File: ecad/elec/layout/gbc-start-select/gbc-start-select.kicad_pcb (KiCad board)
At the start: 2 copper layers, 5 parts

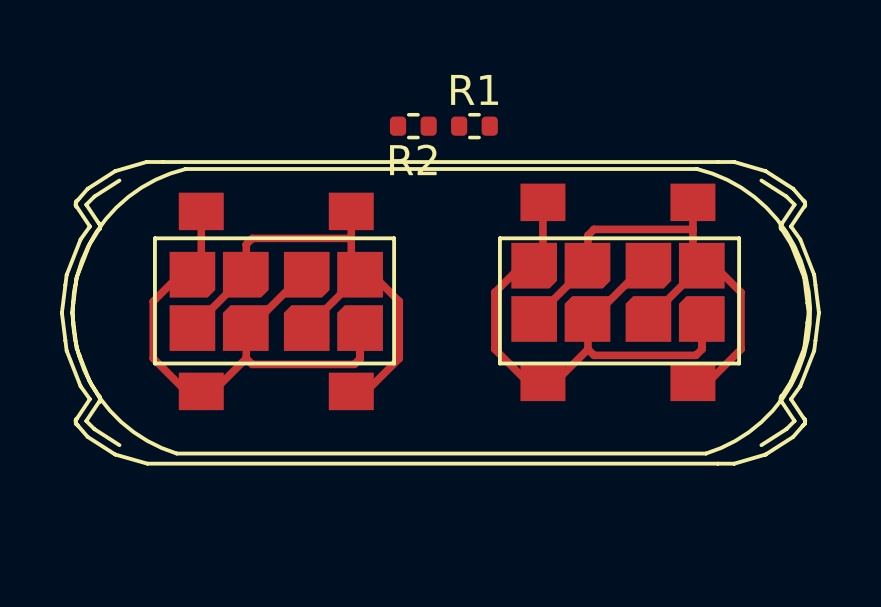
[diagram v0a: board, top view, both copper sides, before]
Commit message: update layouts to use latest footprints and fixed volume buttons and include address pins
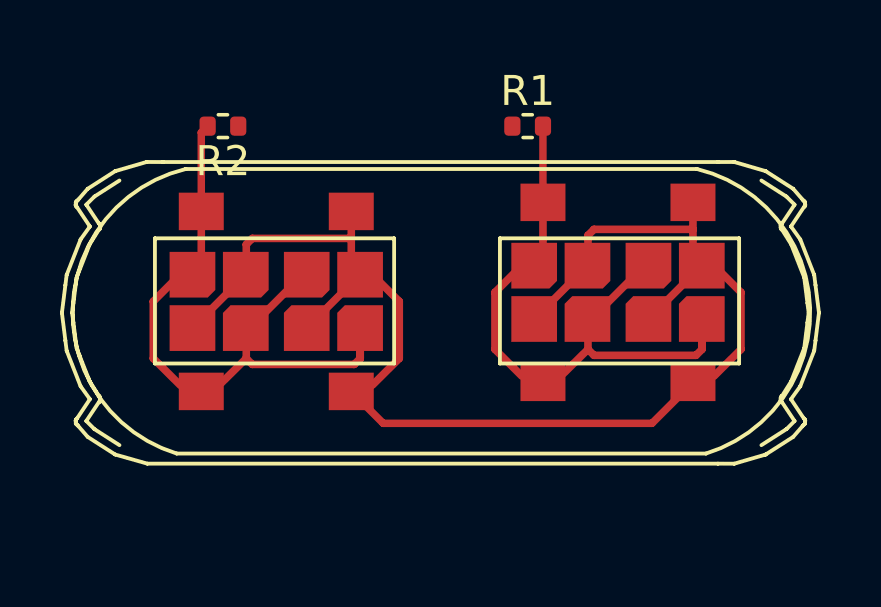
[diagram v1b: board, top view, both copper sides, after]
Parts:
- moved R2 6.35 mm to (166.6, 71.9)
- moved R1 1.77 mm to (176.8, 71.9)
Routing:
- net vcc: track 0.00 -> 12.4 mm
- net select: track 0.00 -> 2.93 mm
- net start: track 0.00 -> 2.54 mm

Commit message: Fix/atopile ecad (#82)
* fix(ecad): Fix bugs in atopile version of the design
* Add missing pullup resistors to AW9523 RSTN and INTN lines
* Fix I/O configuration for AW9523 so that all the inputs go to the same port pins as the previous version of the electronics

* minor cleanup to box3 after update to at 0.2.58

* fix udpate max17038 pullup to properly go to alert line after other fix

* typo

* update layout

* minor update to layout

* fix(buttons): pulldown -> pullup (so they are active low)

* update buttons to be pullup instead of pulldown; change led to be powered off VBUS instead of vbat

* update button footprints - start/select better aligned and all buttons have extra wires to ensure connections

* add net names and ensure packages are specified

* update box-emu-base layout

* update box-emu and box-3-emu layouts

* udpate to kicad 8

* add net name overrides and update all boards

* update atopile action to kicad 8

* comment out blender render
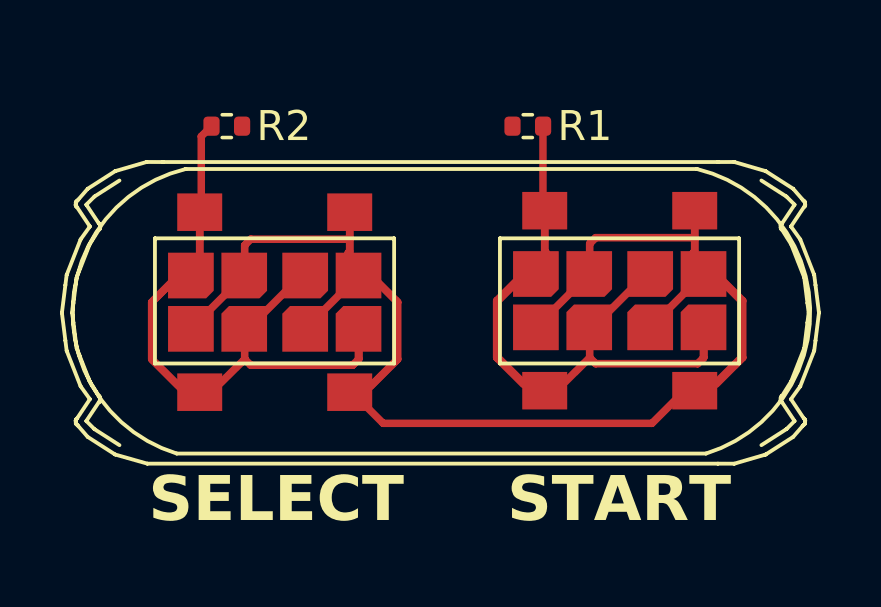
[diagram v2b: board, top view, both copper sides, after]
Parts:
- moved U2 0.28 mm to (179.8, 77.7)
- moved R2 0.13 mm to (166.8, 71.9)
- moved U3 0.06 mm to (168.3, 77.8)
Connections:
- R1 pad 1: gnd -> vcc
- R2 pad 1: gnd -> vcc
- U2 pad 2: vcc -> gnd
- U2 pad 4: vcc -> gnd
- U3 pad 2: vcc -> gnd
- U3 pad 4: vcc -> gnd
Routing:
- net gnd: track 0.00 -> 27.6 mm
- net vcc: track 12.4 -> 0.00 mm
- net select: track 2.93 -> 10.6 mm
- net start: track 2.54 -> 10.1 mm
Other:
- board text added: "SELECT"
- board text added: "START"
